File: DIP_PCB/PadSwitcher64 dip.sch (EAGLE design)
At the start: 15 parts, among them U1 ATMEGA88A-PU

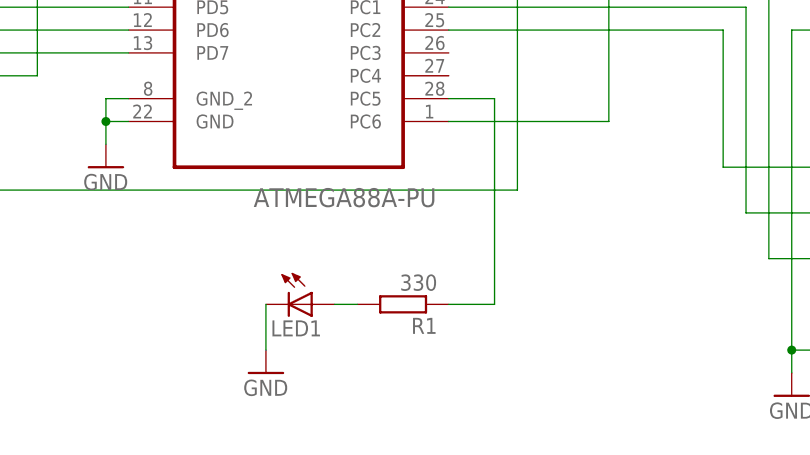
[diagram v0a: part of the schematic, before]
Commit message: Fixed component values on silkscreen.
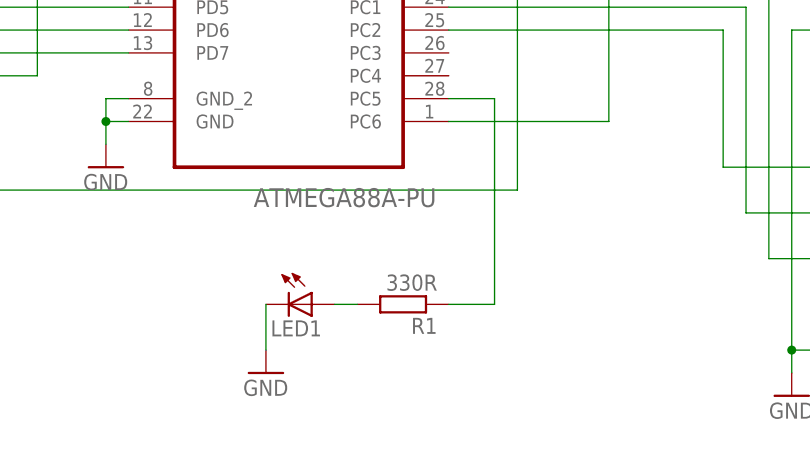
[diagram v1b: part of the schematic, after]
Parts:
- R1: value 330 -> 330R
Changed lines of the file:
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@@
 <part name="SNES_NC2" library="wirepad" deviceset="3,17/1,1" device=""/>
 <part name="SNES_GND" library="wirepad" deviceset="3,17/1,1" device=""/>
-<part name="R1" library="resistor" deviceset="R-EU_" device="0207/10" value="330"/>
+<part name="R1" library="resistor" deviceset="R-EU_" device="0207/10" value="330R"/>
 <part name="P+1" library="supply1" deviceset="+5V" device=""/>
 <part name="P+2" library="supply1" deviceset="+5V" device=""/>

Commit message: Adjusted component positions.
Turns out that there wasn't enough room to mount the straight pin SNES socket properly.  The PCB has been enlarged a smidgen and the AVR and socket have been moved apart a little.
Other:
- note added: "This file is part of PadSwitcher64. PadSwitcher64 is free software / hardware: you can redistribute it and/or modify it under the terms of the GNU General Public License as published by the Free Software Foundation, either version 3 of the License, or (at your option) any later version. PadSwitcher64 is distributed in the hope that it will be useful, but WITHOUT ANY WARRANTY; without even the imp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"
- note removed: "This file is part of PadSwitcher64. PadSwitcher64 is free software: you can redistribute it and/or modify it under the terms of the GNU General Public License as published by the Free Software Foundation, either version 3 of the License, or (at your option) any later version. PadSwitcher64 is distributed in the hope that it will be useful, but WITHOUT ANY WARRANTY; without even the implied warran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"
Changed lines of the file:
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@@
 <plain>
 <text x="27.94" y="-15.24" size="1.27" layer="100">    This file is part of PadSwitcher64.
-    PadSwitcher64 is free software: you can redistribute it and/or modify
+    PadSwitcher64 is free software / hardware: you can redistribute it and/or modify
     it under the terms of the GNU General Public License as published by
     the Free Software Foundation, either version 3 of the License, or
